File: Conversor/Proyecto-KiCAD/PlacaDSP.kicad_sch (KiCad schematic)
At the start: 0 parts

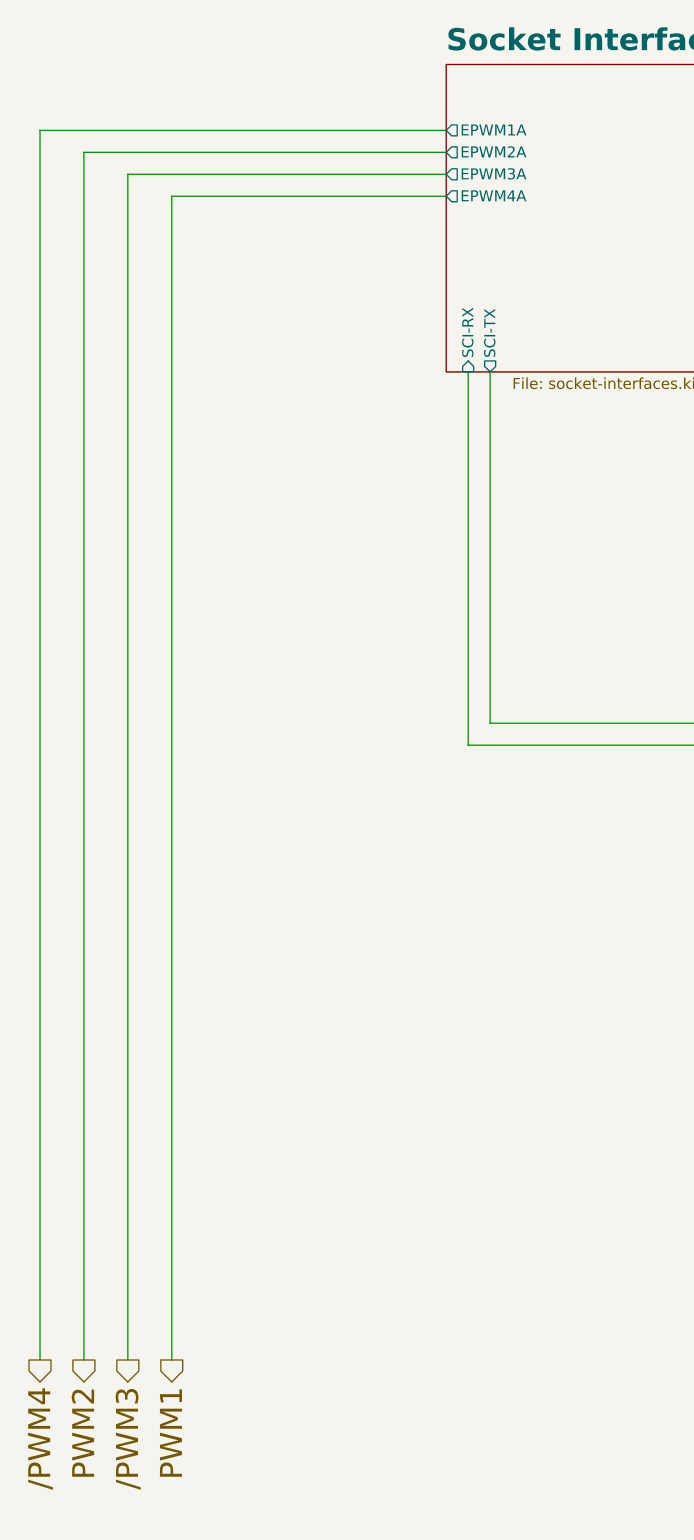
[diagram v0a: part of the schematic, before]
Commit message: Arreglar los primeros dos items marcados por Jorge
- Usar EPWM1A/B y EPWM2A/B para poder usar la función de phase-shift de
los modulos PWM y ahorrarse la sincronización manual
- Agregar diodos de descarga D8 y D9 a la salida de los drivers
- Agregar el Technical Reference Manual del DSP a la bibliografía
(descripción ultra detallada de todas las funciones del DSP)
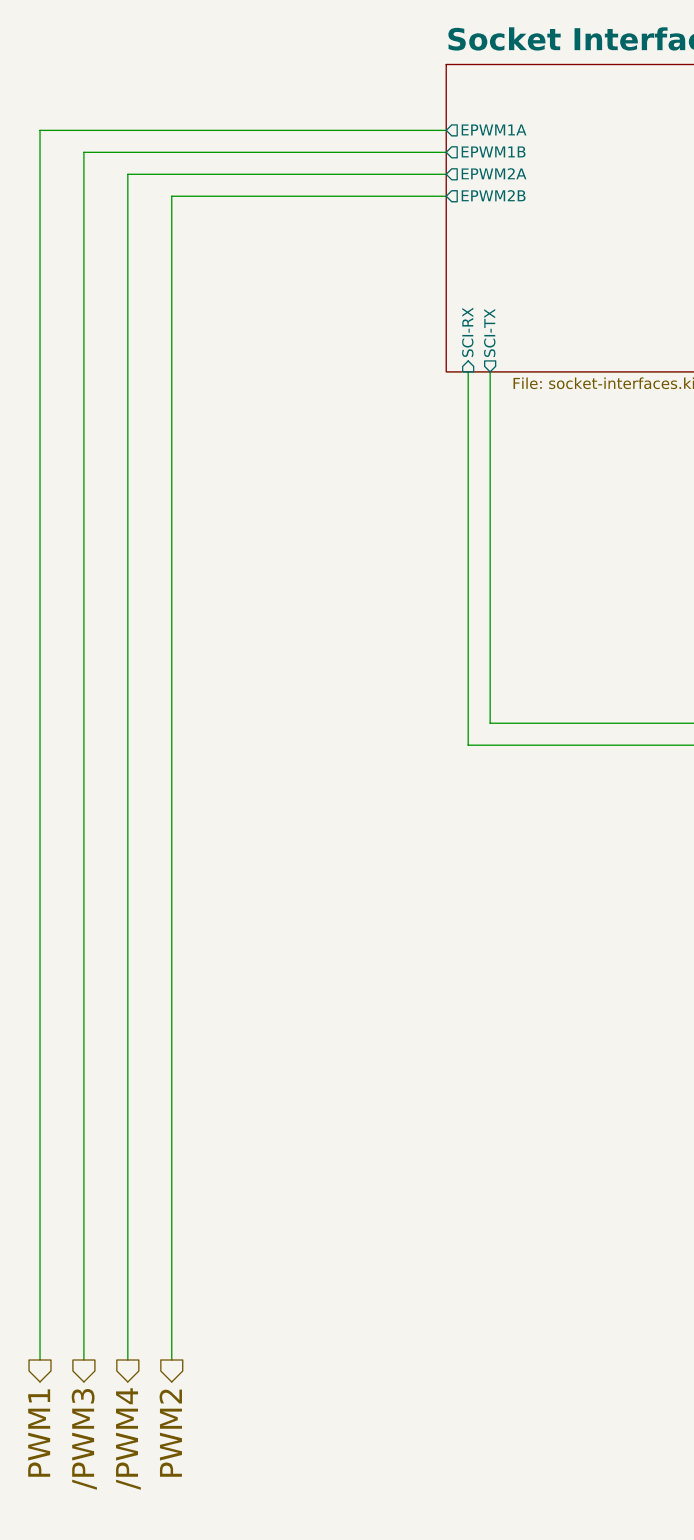
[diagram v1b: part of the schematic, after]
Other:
- sheet Socket Interfaces ports: added EPWM1B, EPWM2B; removed EPWM3A, EPWM4A
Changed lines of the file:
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@@
     (effects (font (size 2.54 2.54)) (justify left))
   )
-  (hierarchical_label "{slash}PWM4" (shape output) (at 25.4 173.99 270)
+  (hierarchical_label "PWM1" (shape output) (at 25.4 173.99 270)
     (effects (font (size 2.54 2.54)) (justify right))
   )
-  (hierarchical_label "{slash}PWM3" (shape output) (at 35.56 173.99 270)
+  (hierarchical_label "{slash}PWM3" (shape output) (at 30.48 173.99 270)
     (effects (font (size 2.54 2.54)) (justify right))
   )
-  (hierarchical_label "PWM2" (shape output) (at 30.48 173.99 270)
+  (hierarchical_label "PWM2" (shape output) (at 40.64 173.99 270)
     (effects (font (size 2.54 2.54)) (justify right))
   )
@@
     (effects (font (size 2.54 2.54)) (justify left))
   )
-  (hierarchical_label "PWM1" (shape output) (at 40.64 173.99 270)
+  (hierarchical_label "{slash}PWM4" (shape output) (at 35.56 173.99 270)
     (effects (font (size 2.54 2.54)) (justify right))
   )
@@
       (effects (font (size 1.27 1.27)) (justify left))
     )
-    (pin "EPWM4A" output (at 72.39 39.37 180)
-      (effects (font (size 1.27 1.27)) (justify left))
-    )
-    (pin "EPWM3A" output (at 72.39 36.83 180)
-      (effects (font (size 1.27 1.27)) (justify left))
-    )
     (pin "EPWM1A" output (at 72.39 31.75 180)
       (effects (font (size 1.27 1.27)) (justify left))
     )
-    (pin "EPWM2A" output (at 72.39 34.29 180)
+    (pin "EPWM2A" output (at 72.39 36.83 180)
       (effects (font (size 1.27 1.27)) (justify left))
     )
@@
       (effects (font (size 1.27 1.27)) (justify right))
     )
+    (pin "EPWM1B" output (at 72.39 34.29 180)
+      (effects (font (size 1.27 1.27)) (justify left))
+    )
+    (pin "EPWM2B" output (at 72.39 39.37 180)
+      (effects (font (size 1.27 1.27)) (justify left))
+    )
   )
